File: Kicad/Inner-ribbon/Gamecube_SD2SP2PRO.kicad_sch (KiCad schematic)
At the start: 2 parts, among them J1 Conn_02x04_Odd_Even, J2 Conn_02x04_Odd_Even

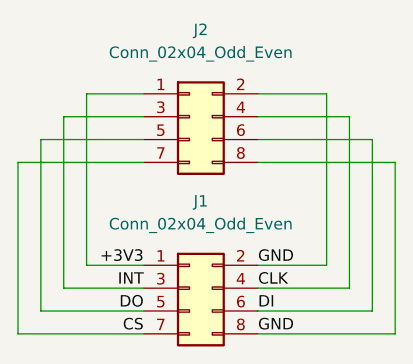
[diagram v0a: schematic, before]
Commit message: fix SD2SP2 connector pinout
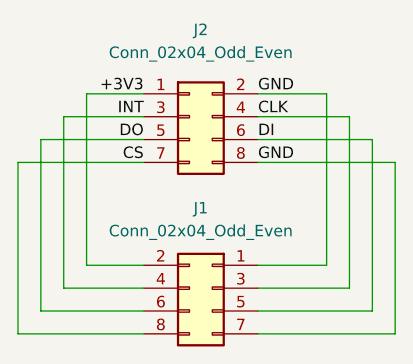
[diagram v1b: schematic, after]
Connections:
- net +3V3: now also J1.2 (Pin_2); no longer J1.1 (Pin_1)
- net CLK: now also J1.3 (Pin_3); no longer J1.4 (Pin_4)
- net CS: now also J1.8 (Pin_8); no longer J1.7 (Pin_7)
- net DI: now also J1.5 (Pin_5); no longer J1.6 (Pin_6)
- net DO: now also J1.6 (Pin_6); no longer J1.5 (Pin_5)
- net GND: now also J1.1 (Pin_1), J1.7 (Pin_7); no longer J1.2 (Pin_2), J1.8 (Pin_8)
- net INT: now also J1.4 (Pin_4); no longer J1.3 (Pin_3)
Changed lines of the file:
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@@
     (stroke (width 0) (type default) (color 0 0 0 0))
   )
-  (label "DO" (at 73.66 87.63 180)
+  (label "DO" (at 73.66 68.58 180)
     (effects (font (size 1.27 1.27)) (justify right bottom))
   )
-  (label "CS" (at 73.66 90.17 180)
+  (label "CS" (at 73.66 71.12 180)
     (effects (font (size 1.27 1.27)) (justify right bottom))
   )
-  (label "INT" (at 73.66 85.09 180)
+  (label "INT" (at 73.66 66.04 180)
     (effects (font (size 1.27 1.27)) (justify right bottom))
   )
-  (label "CLK" (at 86.36 85.09 0)
+  (label "CLK" (at 86.36 66.04 0)
     (effects (font (size 1.27 1.27)) (justify left bottom))
   )
-  (label "+3V3" (at 73.66 82.55 180)
+  (label "+3V3" (at 73.66 63.5 180)
     (effects (font (size 1.27 1.27)) (justify right bottom))
   )
-  (label "GND" (at 86.36 82.55 0)
+  (label "GND" (at 86.36 63.5 0)
     (effects (font (size 1.27 1.27)) (justify left bottom))
   )
-  (label "GND" (at 86.36 90.17 0)
+  (label "GND" (at 86.36 71.12 0)
     (effects (font (size 1.27 1.27)) (justify left bottom))
   )
-  (label "DI" (at 86.36 87.63 0)
+  (label "DI" (at 86.36 68.58 0)
     (effects (font (size 1.27 1.27)) (justify left bottom))
   )
-  (symbol (lib_id "Connector_Generic:Conn_02x04_Odd_Even") (at 78.74 85.09 0) (unit 1)
+  (symbol (lib_id "Connector_Generic:Conn_02x04_Odd_Even") (at 81.28 85.09 0) (mirror y) (unit 1)
     (in_bom yes) (on_board yes) (fields_autoplaced)
-    (property "Reference" "J1" (id 0) (at 80.01 75.438 0))
-    (property "Value" "Conn_02x04_Odd_Even" (id 1) (at 80.01 77.978 0))
-    (property "Footprint" "Connector_PinHeader_2.54mm:PinHeader_2x04_P2.54mm_Horizontal" (id 2) (at 78.74 85.09 0)
+    (property "Reference" "J1" (id 0) (at 80.01 76.2 0))
+    (property "Value" "Conn_02x04_Odd_Even" (id 1) (at 80.01 78.74 0))
+    (property "Footprint" "Connector_PinHeader_2.54mm:PinHeader_2x04_P2.54mm_Horizontal" (id 2) (at 81.28 85.09 0)
       (effects (font (size 1.27 1.27)) hide)
     )
-    (property "Datasheet" "~" (id 3) (at 78.74 85.09 0)
+    (property "Datasheet" "~" (id 3) (at 81.28 85.09 0)
       (effects (font (size 1.27 1.27)) hide)
     )
-    (property "LCSC" "C492432" (id 4) (at 78.74 85.09 0)
+    (property "LCSC" "C492432" (id 4) (at 81.28 85.09 0)
       (effects (font (size 1.27 1.27)) hide)
     )
